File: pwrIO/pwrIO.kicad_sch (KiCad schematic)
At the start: 8 parts, among them J3 VCC_MOTOR, J6 MISC, J7 ENC1, J8 ENC2

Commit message: sch pcb
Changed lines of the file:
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@@
 	)
 	(label "NB_B5"
-		(at 124.46 80.01 180)
+		(at 124.46 73.66 180)
 		(fields_autoplaced yes)
 		(effects
@@
 	)
 	(label "NB_B2"
-		(at 124.46 69.85 180)
+		(at 82.55 62.23 180)
 		(fields_autoplaced yes)
 		(effects
@@
 	)
 	(label "NB_B3"
-		(at 124.46 73.66 180)
+		(at 82.55 82.55 180)
 		(fields_autoplaced yes)
 		(effects
@@
 	)
 	(label "NB_B4"
-		(at 124.46 76.2 180)
+		(at 124.46 67.31 180)
 		(fields_autoplaced yes)
 		(effects
@@
 	)
 	(label "NB_A4"
-		(at 82.55 76.2 180)
+		(at 82.55 69.85 180)
 		(fields_autoplaced yes)
 		(effects
@@
 	)
 	(label "NB_B1"
-		(at 124.46 67.31 180)
+		(at 82.55 76.2 180)
 		(fields_autoplaced yes)
 		(effects
@@
 	)
 	(label "NB_A3"
-		(at 82.55 73.66 180)
+		(at 82.55 80.01 180)
 		(fields_autoplaced yes)
 		(effects
@@
 	)
 	(label "NB_A6"
-		(at 82.55 82.55 180)
+		(at 124.46 62.23 180)
 		(fields_autoplaced yes)
 		(effects
@@
 	)
 	(label "NB_A2"
-		(at 82.55 69.85 180)
+		(at 82.55 73.66 180)
 		(fields_autoplaced yes)
 		(effects
@@
 	)
 	(label "NB_B6"
-		(at 124.46 82.55 180)
+		(at 124.46 80.01 180)
 		(fields_autoplaced yes)
 		(effects
@@
 	)
 	(label "NB_A5"
-		(at 82.55 80.01 180)
+		(at 124.46 76.2 180)
 		(fields_autoplaced yes)
 		(effects
@@
 	)
 	(label "NB_A1"
-		(at 82.55 67.31 180)
-		(fields_autoplaced yes)
-		(effects
+		(at 82.55 22.86 180)
+		(fields_autoplaced yes)
+		(effects

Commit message: sch pcb
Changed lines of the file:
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@@
+	(wire
+		(pts
+			(xy 119.38 69.85) (xy 129.54 69.85)
+		)
+		(stroke
+			(width 0)
+			(type default)
+		)
+	)
 	(wire
 		(pts
@@
 	(wire
 		(pts
-			(xy 124.46 69.85) (xy 129.54 69.85)
-		)
-		(stroke
-			(width 0)
-			(type default)
-		)
-	)
-	(wire
-		(pts
 			(xy 124.46 80.01) (xy 129.54 80.01)
 		)
@@
 	(wire
 		(pts
+			(xy 120.65 82.55) (xy 129.54 82.55)
+		)
+		(stroke
+			(width 0)
+			(type default)
+		)
+	)
+	(wire
+		(pts
 			(xy 82.55 80.01) (xy 87.63 80.01)
 		)
@@
 		(pts
 			(xy 59.69 31.75) (xy 58.42 31.75)
-		)
-		(stroke
-			(width 0)
-			(type default)
-		)
-	)
-	(wire
-		(pts
-			(xy 124.46 82.55) (xy 129.54 82.55)
 		)
 		(stroke
@@
 	)
 	(label "NB_A8"
-		(at 96.52 24.13 0)
+		(at 119.38 69.85 0)
 		(fields_autoplaced yes)
 		(effects
@@
 	)
 	(label "NB_A7"
-		(at 96.52 26.67 0)
+		(at 120.65 82.55 0)
 		(fields_autoplaced yes)
 		(effects
@@
 	)
 	(label "NB_A1"
-		(at 82.55 22.86 180)
-		(fields_autoplaced yes)
-		(effects
+		(at 82.55 67.31 180)
+		(fields_autoplaced yes)
+		(effects

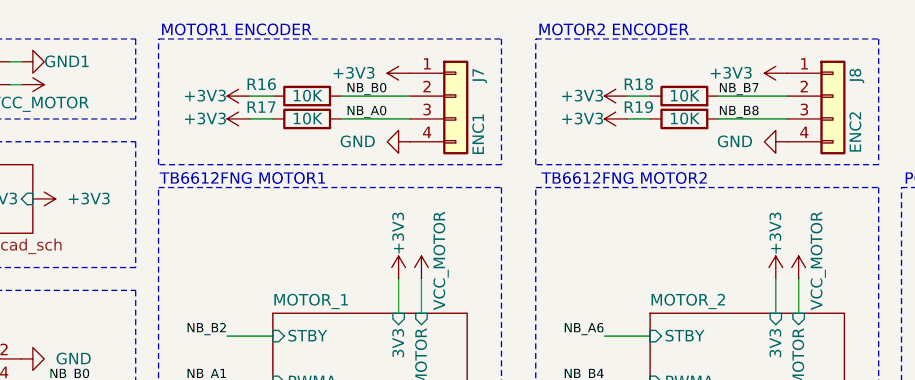
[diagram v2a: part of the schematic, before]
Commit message: Connecting encoder to 2.5V
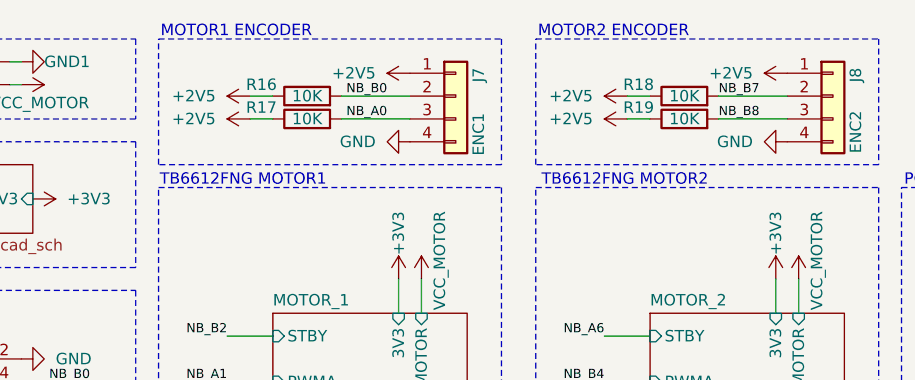
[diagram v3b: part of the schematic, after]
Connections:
- net +2V5: now also J7.1 (Pin_1), J8.1 (Pin_1), R16.1, R17.1, R18.1, R19.1
- net +3V3: no longer J7.1 (Pin_1), J8.1 (Pin_1), R16.1, R17.1, R18.1, R19.1

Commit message: initial connection done
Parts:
- added H1: Logo Intergalaktik, intergalaktik:intergalaktik, symbol Mechanical:MountingHole
- added H2: Logo NLnet, nlnet:nlnet, symbol Mechanical:MountingHole
- added H3: Logo OpenCologne, Cologne:open_cologne, symbol Mechanical:MountingHole
- added H4: Logo Radiona, radiona:radiona, symbol Mechanical:MountingHole

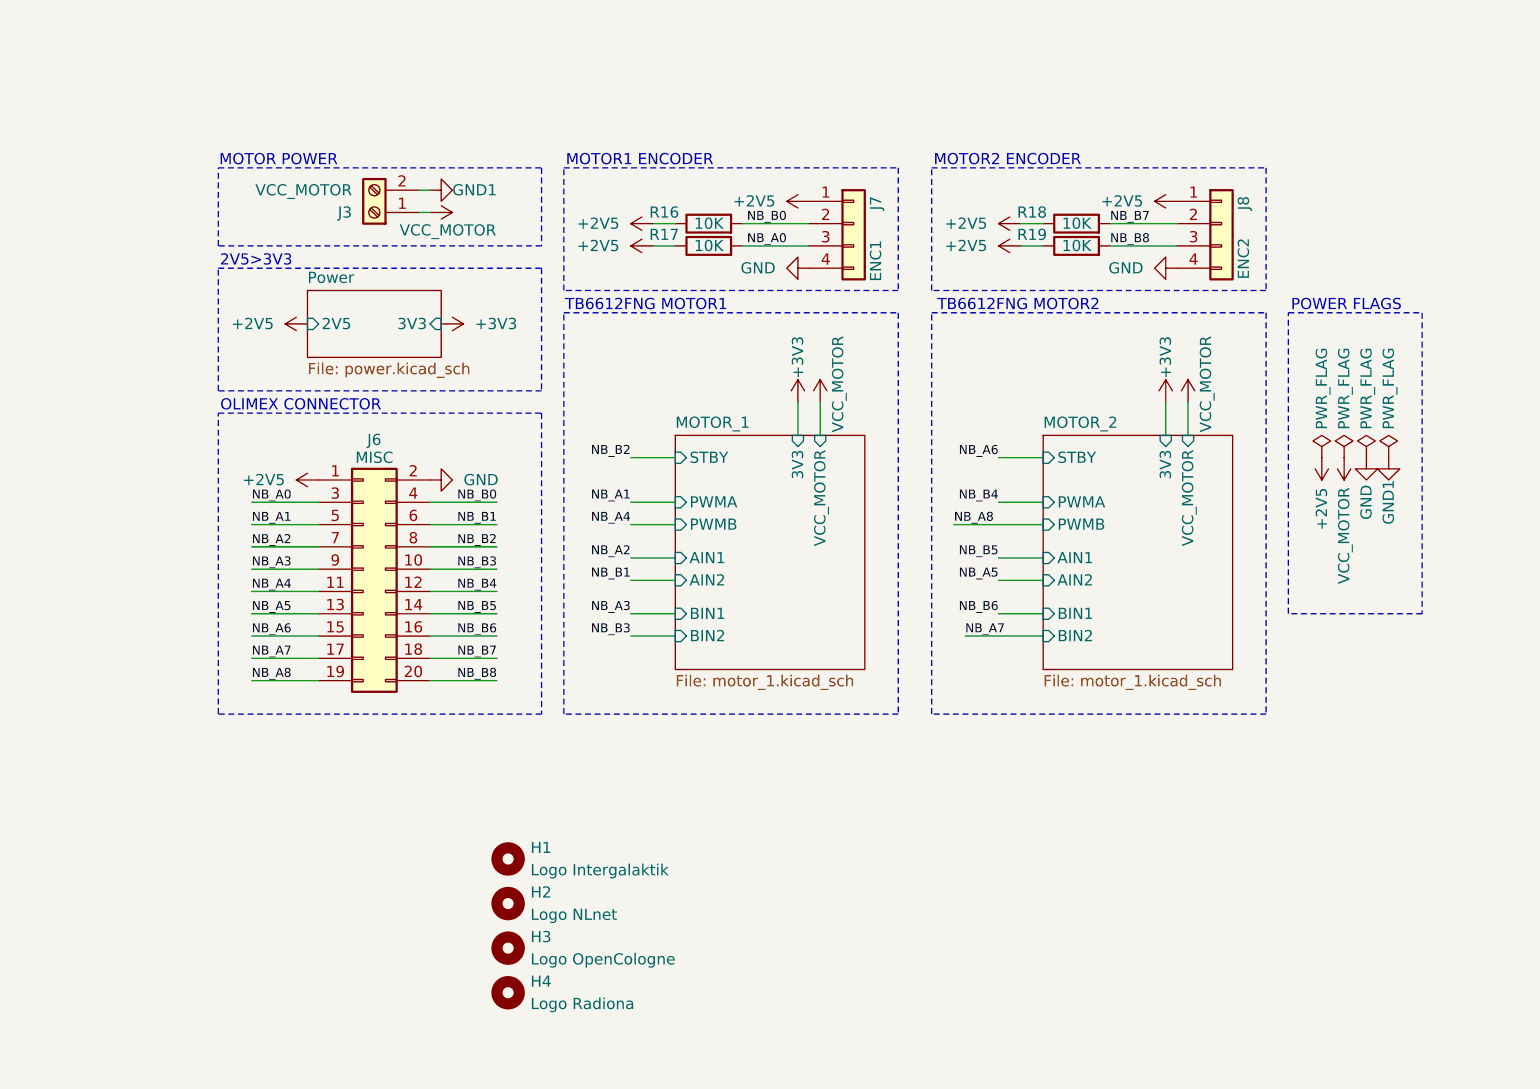
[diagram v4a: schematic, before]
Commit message: Moving schematics to v9 adding more details
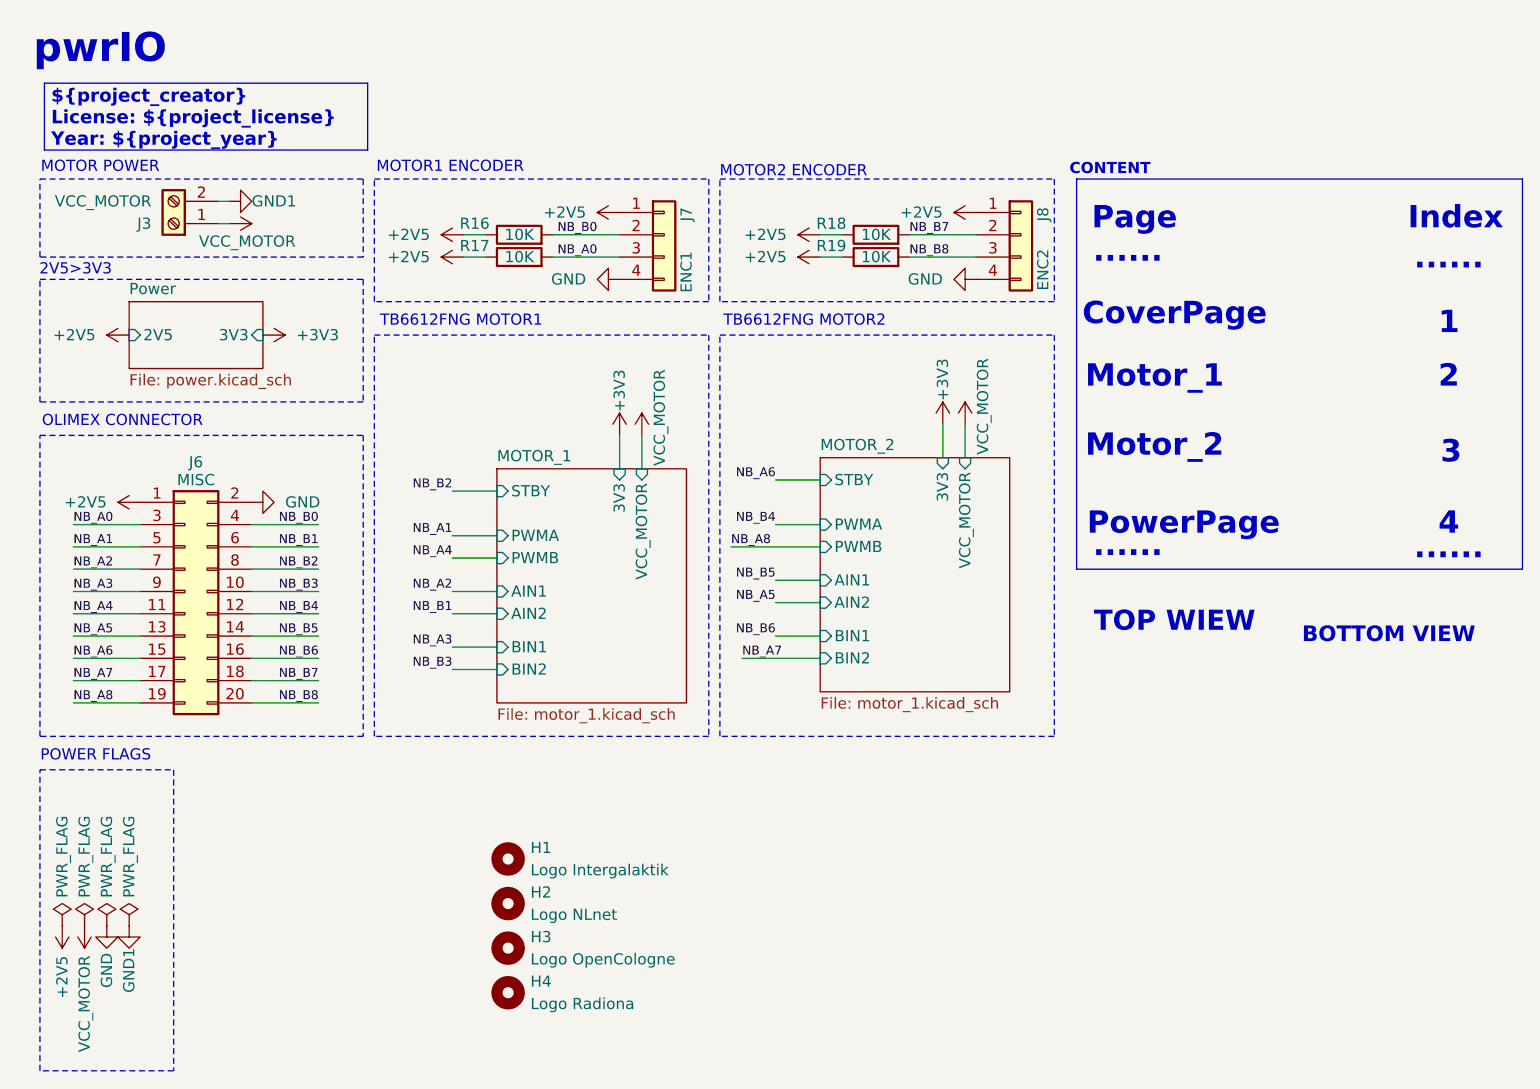
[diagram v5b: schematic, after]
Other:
- note added: "${project_creator} License: ${project_license} Year: ${project_year}"
- note added: "......"
- note added: "1"
- note added: "2"
- note added: "3"
- note added: "4"
- note added: "BOTTOM VIEW"
- note added: "CONTENT"
- note added: "CoverPage"
- note added: "Index"
- note added: "Motor_1"
- note added: "Motor_2"
- note added: "Page"
- note added: "PowerPage"
- note added: "TOP WIEW"
- note added: "pwrIO"
- company: Intergalaktik d.o.o. -> ${project_creator}
- title: Motor driver board -> ${project_name} ${project_version}
- moved on the sheet: J3, J6, J7, J8, R16, R17, R18, R19
